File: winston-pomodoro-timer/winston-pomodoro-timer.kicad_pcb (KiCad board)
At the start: 2 copper layers, 122 x 38 mm, 33 parts, among them J1 Conn_01x05_Pin, J2 Conn_01x05_Pin, J4 Conn_01x04_Pin, J5 Conn_01x06_Pin, U1 ATmega328P-A, Y1 Crystal_GND24

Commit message: finished layout and routing
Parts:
- added C1: 10uF, Capacitor_SMD:C_0603_1608Metric, F.Cu at (166.8, 80.8)
- added C2: 10uF, Capacitor_SMD:C_0603_1608Metric, F.Cu at (168.9, 64.8)
- added C3: 100uF, Capacitor_SMD:C_0805_2012Metric, F.Cu at (174.7, 72.3)
- added C4: 22uF, Capacitor_SMD:C_0603_1608Metric, F.Cu at (157.3, 83.0)
- added J3: Battery_Conn, Connector_PinSocket_2.00mm:PinSocket_1x02_P2.00mm_Vertical, F.Cu at (130.9, 81.5)
- added J6: UJC-HP-3-SMT-TR, UJC-HP-3-SMT-TR:CUI_UJC-HP-3-SMT-TR, F.Cu at (124.0, 67.3)
- added L1: 6.8uH, Inductor_SMD:L_Bourns-SRN4018, F.Cu at (176.5, 67.0)
- added R1: 5.1k, Resistor_SMD:R_0603_1608Metric, F.Cu at (126.2, 71.6)
- added R10: 2.2M, Resistor_SMD:R_0603_1608Metric, F.Cu at (165.2, 66.6)
- added R11: 390K, Resistor_SMD:R_0603_1608Metric, F.Cu at (164.6, 71.2)
- added R12: 1.8M, Capacitor_SMD:C_0603_1608Metric, F.Cu at (170.3, 74.0)
- added R13: 200K, Resistor_SMD:R_0603_1608Metric, F.Cu at (167.9, 74.0)
- added R2: 5.1k, Resistor_SMD:R_0603_1608Metric, F.Cu at (124.0, 71.6)
- added R3: 1M, Resistor_SMD:R_0603_1608Metric, F.Cu at (121.7, 71.6)
- added R4: 590, Resistor_SMD:R_0603_1608Metric, F.Cu at (153.1, 82.8)
- added R5: 1.1k, Resistor_SMD:R_0603_1608Metric, F.Cu at (153.1, 80.5)
- added R6: 1k, Resistor_SMD:R_0603_1608Metric, F.Cu at (155.8, 77.8)
- added R7: 100k, Resistor_SMD:R_0603_1608Metric, F.Cu at (166.0, 78.7)
- added R8: 10k, Resistor_SMD:R_0603_1608Metric, F.Cu at (163.8, 83.2)
- added R9: 200K, Resistor_SMD:R_0603_1608Metric, F.Cu at (169.2, 76.6)
- added SW2: SW_SPDT, Button_Switch_THT:SW_Slide_1P2T_CK_OS102011MS2Q, F.Cu at (136.2, 68.7)
- added U2: BQ24075RGT, Package_DFN_QFN:VQFN-16-1EP_3x3mm_P0.5mm_EP1.6x1.6mm, F.Cu at (159.9, 80.1)
- added U3: TPS61092RSAR, TPS61092RSAR:CONV_TPS61092RSAR, F.Cu at (169.4, 69.1)
- 100nF1, 100nF10, 100nF11, 100nF12, 100nF2, 100nF3, 100nF4, 100nF5, 100nF6, 100nF7, 100nF8, 100nF9, 22pF1, 22pF2: footprint Capacitor_SMD:C_0805_2012Metric_Pad1.18x1.45mm_HandSolder -> Capacitor_SMD:C_0603_1608Metric
- moved 100nF1 0.46 mm to (201.3, 70.0)
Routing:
- net /BAT_V_OUT: track 0.00 -> 64.7 mm, vias 0 -> 2
- net /+V_BAT: track 0.00 -> 48.0 mm
- net /+V_USB: track 0.00 -> 45.8 mm
- net GND: track 16.0 -> 49.6 mm, vias 16 -> 83
- net /Boost_EN: track 0.00 -> 31.7 mm, vias 0 -> 1
- net Net-(J6-SHIELD-PadS1): track 0.00 -> 20.5 mm
- net +5V: track 275.0 -> 288.8 mm
- net Net-(U3-LBI): track 0.00 -> 8.59 mm
- net Net-(U2-ISET): track 0.00 -> 6.58 mm, vias 0 -> 2
- net Net-(U3-FB): track 0.00 -> 6.25 mm
- net Net-(L1-Pad2): track 0.00 -> 5.79 mm
- net Net-(U2-ILIM): track 0.00 -> 4.73 mm
- net Net-(U2-~{CE}): track 0.00 -> 4.51 mm
- net Net-(J6-CC1): track 0.00 -> 4.12 mm
- net Net-(J6-CC2): track 0.00 -> 3.63 mm
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- added copper zone on F.Cu, net +5V
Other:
- outline, holes or cut-outs redrawn
- board text added: "+5V"
- board text added: "A0 A1 A2 A3 A6 A7"
- board text added: "C"
- board text added: "COMMON"
- board text added: "D"
- board text added: "D3 D4 D5 D6 D7"
- board text added: "GND"
- board text added: "SCL"
- board text added: "SDA"
- board text added: "SWT"

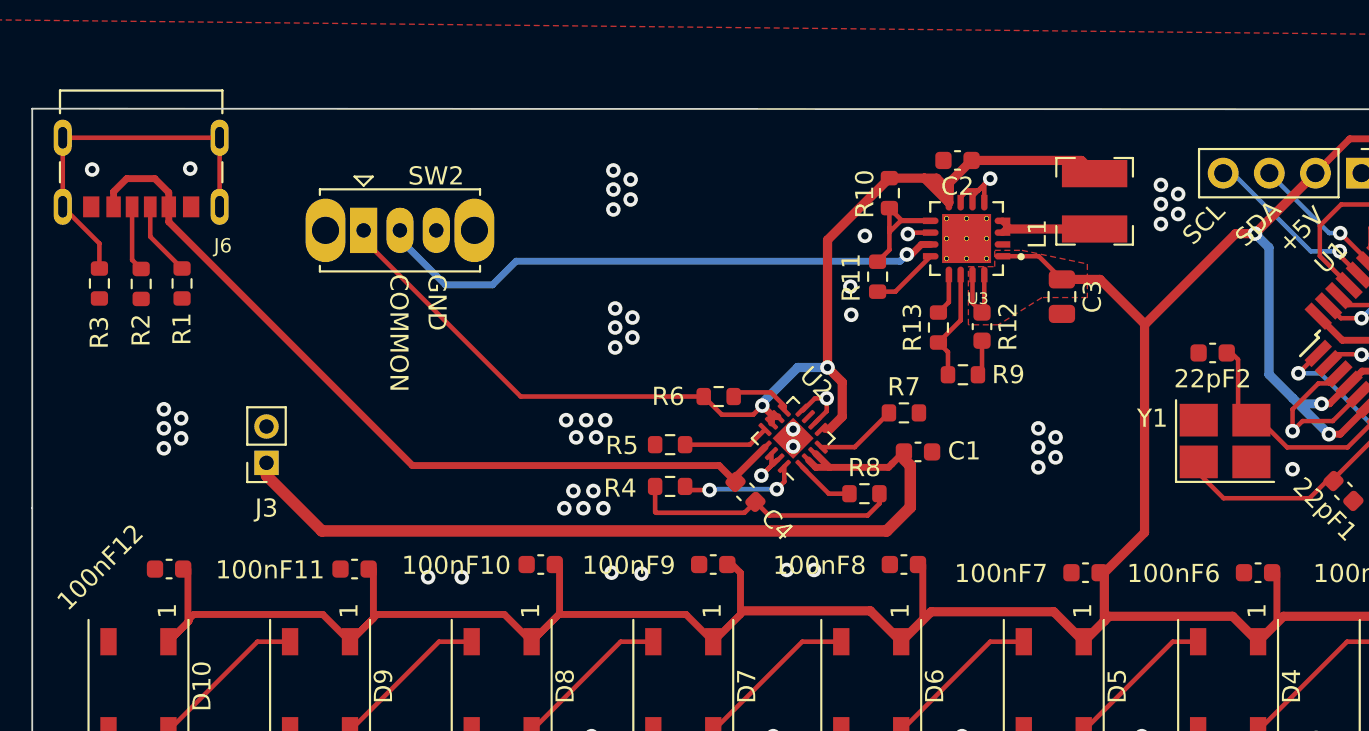
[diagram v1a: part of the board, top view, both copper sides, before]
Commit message: added battery override jumpers
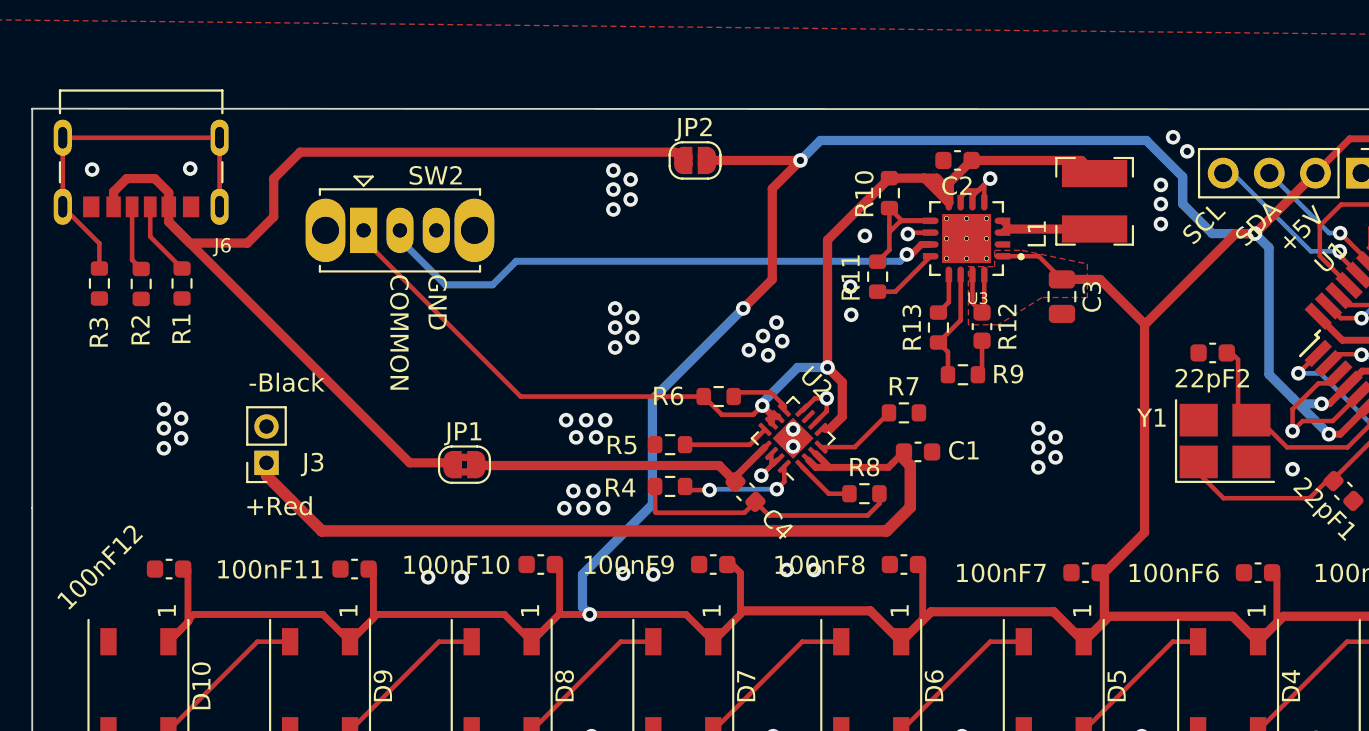
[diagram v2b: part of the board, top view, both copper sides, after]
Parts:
- added JP1: Jumper_2_Bridged, Jumper:SolderJumper-2_P1.3mm_Bridged2Bar_RoundedPad1.0x1.5mm, F.Cu at (141.8, 81.5)
- added JP2: Jumper_2_Open, Jumper:SolderJumper-2_P1.3mm_Open_RoundedPad1.0x1.5mm, F.Cu at (154.5, 64.8)
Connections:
- J6 pad A9: /+V_USB -> Net-(JP1-A)
- J6 pad B9: /+V_USB -> Net-(JP1-A)
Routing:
- net +5V: track 288.8 -> 352.6 mm, vias 3 -> 6
- net Net-(JP1-A): track 0.00 -> 59.6 mm
- net /+V_USB: track 45.8 -> 17.3 mm
- net GND: vias 83 -> 88
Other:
- board text added: "+Red"
- board text added: "-Black"

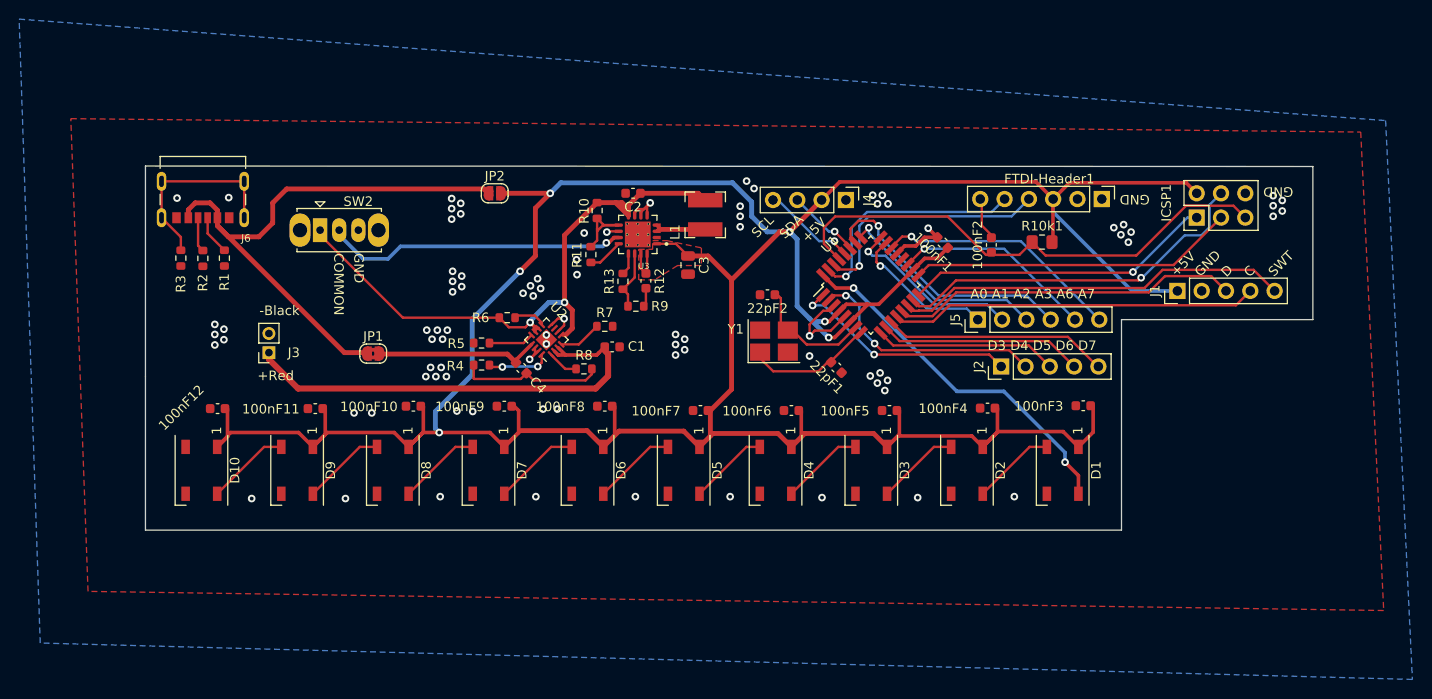
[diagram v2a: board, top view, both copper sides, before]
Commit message: added rounded corners
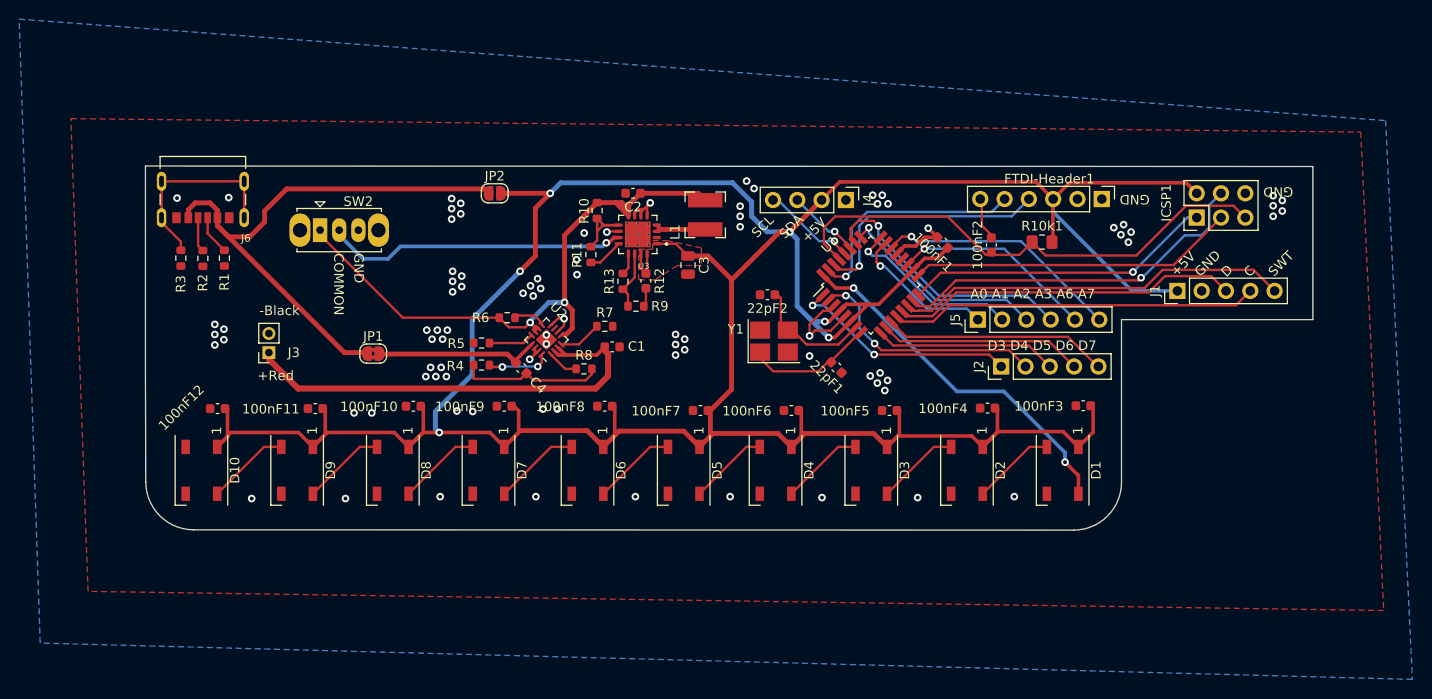
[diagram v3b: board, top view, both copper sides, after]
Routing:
- net Net-(JP1-A): track 59.6 -> 59.0 mm
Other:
- outline, holes or cut-outs redrawn
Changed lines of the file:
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@@
       (net 47 "Net-(J6-SHIELD-PadS1)") (pinfunction "SHIELD") (pintype "passive") (solder_mask_margin 0.102))
   )
-  (gr_line (start 220 100) (end 220 78)
+  (gr_line (start 220.000002 95) (end 220 78)
     (stroke (width 0.1) (type default)) (layer "Edge.Cuts"))
   (gr_line (start 240 62) (end 118 61.95)
@@
   (gr_line (start 240 78) (end 240 62)
     (stroke (width 0.1) (type default)) (layer "Edge.Cuts"))
+  (gr_arc (start 220.000002 95) (mid 218.535535 98.535535) (end 214.999999 100)
+    (stroke (width 0.1) (type default)) (layer "Edge.Cuts"))
   (gr_line (start 220 78) (end 240 78)
     (stroke (width 0.1) (type default)) (layer "Edge.Cuts"))
-  (gr_line (start 118 83.95) (end 118 100)
-    (stroke (width 0.1) (type default)) (layer "Edge.Cuts"))
-  (gr_line (start 118 100) (end 220 100)
+  (gr_line (start 118 83.95) (end 118.035535 94.964465)
+    (stroke (width 0.1) (type default)) (layer "Edge.Cuts"))
+  (gr_arc (start 123.035534 99.964467) (mid 119.499999 98.5) (end 118.035535 94.964465)
+    (stroke (width 0.1) (type default)) (layer "Edge.Cuts"))
+  (gr_line (start 123.035534 99.964467) (end 214.999999 100)
     (stroke (width 0.1) (type default)) (layer "Edge.Cuts"))
   (gr_line (start 118 61.95) (end 118 83.95)
@@
   (segment (start 123.5 70.275) (end 124 70.775) (width 0.254) (layer "F.Cu") (net 46))
   (segment (start 123.5 67.355) (end 123.5 70.275) (width 0.254) (layer "F.Cu") (net 46))
-  (segment (start 121.7 70.75) (end 121.7 69.37) (width 0.254) (layer "F.Cu") (net 47))
+  (segment (start 121.7 70.75) (end 121.7 69.85) (width 0.254) (layer "F.Cu") (net 47))
   (segment (start 119.68 63.55) (end 128.32 63.55) (width 0.254) (layer "F.Cu") (net 47))
+  (segment (start 119.68 67.83) (end 119.68 67.35) (width 0.254) (layer "F.Cu") (net 47))
   (segment (start 119.68 67.35) (end 119.68 63.55) (width 0.254) (layer "F.Cu") (net 47))
-  (segment (start 121.7 69.37) (end 119.68 67.35) (width 0.254) (layer "F.Cu") (net 47))
+  (segment (start 121.7 69.85) (end 119.68 67.83) (width 0.254) (layer "F.Cu") (net 47))
   (segment (start 128.32 63.55) (end 128.32 67.35) (width 0.254) (layer "F.Cu") (net 47))
   (segment (start 159.413864 82.486136) (end 159 82.9) (width 0.254) (layer "F.Cu") (net 48))
@@
   (segment (start 170.3 74.725) (end 170.250002 74.725) (width 0.254) (layer "F.Cu") (net 58))
   (segment (start 170.3 76.375) (end 170.075 76.6) (width 0.254) (layer "F.Cu") (net 58))
-  (segment (start 153.394277 64.344277) (end 153.85 64.8) (width 0.508) (layer "F.Cu") (net 59))
   (segment (start 125.52 67.355) (end 125.52 66.57) (width 0.508) (layer "F.Cu") (net 59))
   (segment (start 123.206 65.8) (end 122.48 66.526) (width 0.508) (layer "F.Cu") (net 59))
   (segment (start 141.05 81.45) (end 141.15 81.55) (width 0.508) (layer "F.Cu") (net 59))
-  (segment (start 131.3 65.8) (end 132.755723 64.344277) (width 0.508) (layer "F.Cu") (net 59))
+  (segment (start 128.9 69.35) (end 130.45 67.8) (width 0.508) (layer "F.Cu") (net 59))
   (segment (start 125.52 68.184) (end 126.686 69.35) (width 0.508) (layer "F.Cu") (net 59))
   (segment (start 122.48 66.526) (end 122.48 67.355) (width 0.508) (layer "F.Cu") (net 59))
   (segment (start 124.75 65.8) (end 123.206 65.8) (width 0.508) (layer "F.Cu") (net 59))
-  (segment (start 126.686 69.35) (end 129.85 69.35) (width 0.508) (layer "F.Cu") (net 59))
+  (segment (start 132.755723 64.344277) (end 153.394277 64.344277) (width 0.508) (layer "F.Cu") (net 59))
   (segment (start 138.786 81.45) (end 141.05 81.45) (width 0.508) (layer "F.Cu") (net 59))
+  (segment (start 126.686 69.35) (end 128.9 69.35) (width 0.508) (layer "F.Cu") (net 59))
+  (segment (start 130.45 66.65) (end 132.755723 64.344277) (width 0.508) (layer "F.Cu") (net 59))
   (segment (start 125.52 68.184) (end 138.786 81.45) (width 0.508) (layer "F.Cu") (net 59))
   (segment (start 125.52 66.57) (end 124.75 65.8) (width 0.508) (layer "F.Cu") (net 59))
-  (segment (start 131.3 67.9) (end 131.3 65.8) (width 0.508) (layer "F.Cu") (net 59))
-  (segment (start 132.755723 64.344277) (end 153.394277 64.344277) (width 0.508) (layer "F.Cu") (net 59))
+  (segment (start 153.394277 64.344277) (end 153.85 64.8) (width 0.508) (layer "F.Cu") (net 59))
+  (segment (start 130.45 67.8) (end 130.45 66.65) (width 0.508) (layer "F.Cu") (net 59))
   (segment (start 125.52 67.355) (end 125.52 68.184) (width 0.508) (layer "F.Cu") (net 59))
-  (segment (start 129.85 69.35) (end 131.3 67.9) (width 0.508) (layer "F.Cu") (net 59))
   (zone (net 1) (net_name "GND") (layer "F.Cu") (hatch edge 0.5)
     (connect_pads (clearance 0.5))
